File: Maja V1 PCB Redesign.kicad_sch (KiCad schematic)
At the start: 0 parts

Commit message: Add component
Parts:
- added F?: Polyfuse_Small, symbol Device:Polyfuse_Small
- added J1: TYPE-C-31-M-12, Keyboard Component:HRO_TYPE-C-31-M-12, symbol TYPE-C-31-M-12:TYPE-C-31-M-12
- added S?: SKQGAFE010, SW_SKQGAFE010, symbol SKQGAFE010:SKQGAFE010
- added U?: PRTR5V0U2X, symbol random-keyboard-parts:PRTR5V0U2X
- added Y?: Crystal_GND24_Small, symbol Device:Crystal_GND24_Small
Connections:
- new net: J1.S1 (SHIELD), J1.S2 (SHIELD), J1.S3 (SHIELD), J1.S4 (SHIELD)
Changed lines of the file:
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@@
-(kicad_sch (version 20210621) (generator eeschema)
+(kicad_sch (version 20211123) (generator eeschema)
   (paper "A4")
+  (symbol (lib_id "TYPE-C-31-M-12:TYPE-C-31-M-12") (at 63.5 78.74 0) (unit 1)
+    (in_bom yes) (on_board yes) (fields_autoplaced)
+    (property "Reference" "J1" (id 0) (at 63.5 60.96 0))
+    (property "Value" "TYPE-C-31-M-12" (id 1) (at 63.5 63.5 0))
+    (property "Footprint" "Keyboard Component:HRO_TYPE-C-31-M-12" (id 2) (at 90.17 50.8 0)
+      (effects (font (size 1.27 1.27)) (justify left bottom) hide)
+    )
+    (property "Datasheet" "" (id 3) (at 63.5 78.74 0)
+      (effects (font (size 1.27 1.27)) (justify left bottom) hide)
+    )
+    (property "MAXIMUM_PACKAGE_HEIGHT" "3.31mm" (id 4) (at 95.25 55.88 0)
+      (effects (font (size 1.27 1.27)) (justify left bottom) hide)
+    )
+    (property "MANUFACTURER" "HRO Electronics" (id 5) (at 93.98 57.15 0)
+      (effects (font (size 1.27 1.27)) (justify left bottom) hide)
+    )
+    (property "PARTREV" "A" (id 6) (at 63.5 78.74 0)
+      (effects (font (size 1.27 1.27)) (justify left bottom) hide)
+    )
+    (property "STANDARD" "Manufacturer Recommendations" (id 7) (at 91.44 53.34 0)
+      (effects (font (size 1.27 1.27)) (justify left bottom) hide)
+    )
+    (pin "A1B12")
+    (pin "A4B9")
+    (pin "A5")
+    (pin "A6")
+    (pin "A7")
+    (pin "A8")
+    (pin "B1A12")
+    (pin "B4A9")
+    (pin "B5")
+    (pin "B6")
+    (pin "B7")
+    (pin "B8")
+    (pin "S1")
+    (pin "S2")
+    (pin "S3")
+    (pin "S4")
+  )
+  (symbol (lib_id "Device:Polyfuse_Small") (at 113.03 58.42 0) (unit 1)
+    (in_bom yes) (on_board yes) (fields_autoplaced)
+    (property "Reference" "F?" (id 0) (at 115.57 57.1499 0)
+      (effects (font (size 1.27 1.27)) (justify left))
+    )
+    (property "Value" "Polyfuse_Small" (id 1) (at 115.57 59.6899 0)
+      (effects (font (size 1.27 1.27)) (justify left))
+    )
+    (property "Footprint" "" (id 2) (at 114.3 63.5 0)
+      (effects (font (size 1.27 1.27)) (justify left) hide)
+    )
+    (property "Datasheet" "~" (id 3) (at 113.03 58.42 0)
+      (effects (font (size 1.27 1.27)) hide)
+    )
+    (pin "1")
+    (pin "2")
+  )
+  (symbol (lib_id "SKQGAFE010:SKQGAFE010") (at 127 76.2 0) (unit 1)
+    (in_bom yes) (on_board yes) (fields_autoplaced)
+    (property "Reference" "S?" (id 0) (at 127 66.04 0))
+    (property "Value" "SKQGAFE010" (id 1) (at 127 68.58 0))
+    (property "Footprint" "SW_SKQGAFE010" (id 2) (at 127 76.2 0)
+      (effects (font (size 1.27 1.27)) (justify left bottom) hide)
+    )
+    (property "Datasheet" "" (id 3) (at 127 76.2 0)
+      (effects (font (size 1.27 1.27)) (justify left bottom) hide)
+    )
+    (property "PART_REV" "B1" (id 4) (at 127 76.2 0)
+      (effects (font (size 1.27 1.27)) (justify left bottom) hide)
+    )
+    (property "STANDARD" "MANUFACTURER RECOMMENDATIONS" (id 5) (at 127 76.2 0)
+      (effects (font (size 1.27 1.27)) (justify left bottom) hide)
+    )
+    (property "MANUFACTURER" "ALPS" (id 6) (at 127 76.2 0)
+      (effects (font (size 1.27 1.27)) (justify left bottom) hide)
+    )
+    (pin "1")
+    (pin "2")
+    (pin "3")
+    (pin "4")
+  )
+  (symbol (lib_id "random-keyboard-parts:PRTR5V0U2X") (at 162.56 77.47 0) (unit 1)
+    (in_bom yes) (on_board yes) (fields_autoplaced)
+    (property "Reference" "U?" (id 0) (at 162.56 69.85 0)
+      (effects (font (size 1.524 1.524)))
+    )
+    (property "Value" "PRTR5V0U2X" (id 1) (at 162.56 73.66 0)
+      (effects (font (size 1.524 1.524)))
+    )
+    (property "Footprint" "" (id 2) (at 162.56 77.47 0)
+      (effects (font (size 1.524 1.524)) hide)
+    )
+    (property "Datasheet" "" (id 3) (at 162.56 77.47 0)
+      (effects (font (size 1.524 1.524)) hide)
+    )
+    (pin "1")
+    (pin "2")
+    (pin "3")
+    (pin "4")
+  )
+  (symbol (lib_id "Device:Crystal_GND24_Small") (at 140.97 45.72 0) (unit 1)
+    (in_bom yes) (on_board yes) (fields_autoplaced)
+    (property "Reference" "Y?" (id 0) (at 153.67 41.5798 0))
+    (property "Value" "Crystal_GND24_Small" (id 1) (at 153.67 44.1198 0))
+    (property "Footprint" "" (id 2) (at 140.97 45.72 0)
+      (effects (font (size 1.27 1.27)) hide)
+    )
+    (property "Datasheet" "~" (id 3) (at 140.97 45.72 0)
+      (effects (font (size 1.27 1.27)) hide)
+    )
+    (pin "1")
+    (pin "2")
+    (pin "3")
+    (pin "4")
+  )
   (sheet_instances
     (path "/" (page "1"))
   )
+  (symbol_instances
+    (path "/6babdcfa-df8d-4f52-842d-5f83ac30f7ac"
+      (reference "F?") (unit 1) (value "Polyfuse_Small") (footprint "")
+    )
+    (path "/31ab6056-77a7-4722-90c3-619f8073b0cc"
+      (reference "J1") (unit 1) (value "TYPE-C-31-M-12") (footprint "Keyboard Component:HRO_TYPE-C-31-M-12")
+    )
+    (path "/9951f9e8-2210-4dce-85a6-75dc798cb094"
+      (reference "S?") (unit 1) (value "SKQGAFE010") (footprint "SW_SKQGAFE010")
+    )
+    (path "/a052622e-11d7-4538-81c6-88b46570ea55"
+      (reference "U?") (unit 1) (value "PRTR5V0U2X") (footprint "")
+    )
+    (path "/ad1125ce-e48c-4b3a-afc6-cc3f494ae7c7"
+      (reference "Y?") (unit 1) (value "Crystal_GND24_Small") (footprint "")
+    )
+  )
 )

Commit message: Atmega Schematic
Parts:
- added C? (x2): 22p, symbol Device:C_Small
- added C? (x5): 0.1u, symbol Device:C_Small
- added C?: 1u, symbol Device:C_Small
- added J?: AVR-ISP-6, symbol Connector:AVR-ISP-6
- added R? (x2): 5.1k, symbol Device:R_Small
- added R? (x2): 10k, symbol Device:R_Small
- added R? (x2): 22, symbol Device:R_Small
- added U1: ATmega32U4-M, Package_DFN_QFN:QFN-44-1EP_7x7mm_P0.5mm_EP5.2x5.2mm, symbol MCU_Microchip_ATmega:ATmega32U4-M
- F?: value Polyfuse_Small -> 500m
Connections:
- net GND: now reaches J1.A1B12 (GND)
- net GND: now also J1.B1A12 (GND), J1.S1 (SHIELD), J1.S2 (SHIELD), J1.S3 (SHIELD), J1.S4 (SHIELD), S?.3, U?.1 (GND), Y?.2, Y?.4, C?.2, C?.2, C?.2, C?.2, C?.2, C?.2, C?.2, C?.2, J?.6 (GND), R?.2, R?.2, R?.2, U1.15 (GND), U1.23 (GND), U1.35 (GND), U1.43 (GND), U1.45 (GND), U1.5 (UGND)
- net VCC: now reaches J1.A4B9 (VBUS)
- net VCC: now also F?.2, J1.B4A9 (VBUS), U?.4 (VCC)
- net at J1.A5 (CC1): now also R?.1
- net at J1.A6 (DP1): now also J1.B6 (DP2), U?.2 (IO1), R?.1
- net at J1.A7 (DN1): now also J1.B7 (DN2), U?.3 (IO2), R?.1
- net at J1.B5 (CC2): now also R?.1
- net +5V: now reaches F?.1
- net +5V: now also C?.1, C?.1, C?.1, C?.1, C?.1, J?.2 (VCC), R?.1, U1.14 (VCC), U1.2 (UVCC), U1.24 (AVCC), U1.34 (VCC), U1.44 (AVCC)
- net RESET: now reaches S?.2
- net RESET: now also J?.5 (~{RST}), R?.2, U1.13 (~{RESET})
- net XTAL1: now reaches Y?.1
- net XTAL1: now also C?.1, U1.17 (XTAL1)
- net XTAL2: now reaches Y?.3
- net XTAL2: now also C?.1, U1.16 (XTAL2)
- new net: R?.1, U1.33 (~{HWB}/PE2)
- new net: C?.1, U1.6 (UCAP)
- new net D+: R?.2, U1.4 (D+)
- new net D-: R?.2, U1.3 (D-)
- new net MISO: J?.1 (MISO), U1.11 (PB3)
- new net MOSI: J?.4 (MOSI), U1.10 (PB2)
- new net SCK: J?.3 (SCK), U1.9 (PB1)
- no-connect marks 0 -> 5
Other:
- moved on the sheet: F?, J1, S?, U?, Y?

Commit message: Finish Wiring
Schematic wiring
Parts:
- gave numbers to parts that had none: 19
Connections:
- net +5V: now also U1.7 (VBUS)
- net ROW0: now reaches U1.1 (PE6)
- net ROW 2: now reaches U1.12 (PB7)
- net COL0: now reaches U1.18 (PD0)
- net COL1: now reaches U1.19 (PD1)
- net COL2: now reaches U1.20 (PD2)
- net COL3: now reaches U1.21 (PD3)
- net COL5: now reaches U1.22 (PD5)
- net COL4: now reaches U1.25 (PD4)
- net COL6: now reaches U1.26 (PD6)
- net ROW4: now reaches U1.28 (PB4)
- net ROW3: now reaches U1.29 (PB5)
- net COL13: now reaches U1.30 (PB6)
- net COL15: now reaches U1.31 (PC6)
- net COL14: now reaches U1.32 (PC7)
- net COL12: now reaches U1.36 (PF7)
- net COL11: now reaches U1.37 (PF6)
- net COL10: now reaches U1.38 (PF5)
- net COL9: now reaches U1.39 (PF4)
- net COL8: now reaches U1.40 (PF1)
- net COL7: now reaches U1.41 (PF0)
- net ROW1: now reaches U1.8 (PB0)
- no-connect marks 5 -> 6
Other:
- added sheet Matrix (Matrix.kicad_sch)

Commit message: fixed footprint & Symbol
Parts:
- C1, C2, C3, C4, C5, C6, C7, C8: footprint (none) -> Capacitor_SMD:C_0805_2012Metric_Pad1.18x1.45mm_HandSolder
- F1: footprint (none) -> Fuse:Fuse_1206_3216Metric_Pad1.42x1.75mm_HandSolder
- J2: footprint (none) -> random-keyboard-parts:Reset_Pretty
- R1, R2, R3, R4, R5, R6: footprint (none) -> Resistor_SMD:R_0805_2012Metric_Pad1.20x1.40mm_HandSolder
- U2: footprint (none) -> random-keyboard-parts:SOT143B
- Y1: footprint (none) -> Crystal:Crystal_SMD_3225-4Pin_3.2x2.5mm

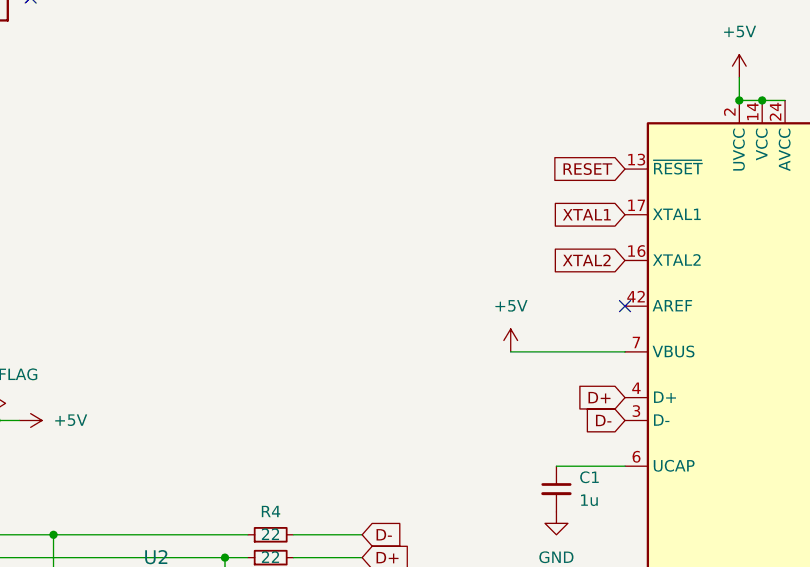
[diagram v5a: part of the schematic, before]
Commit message: add JST
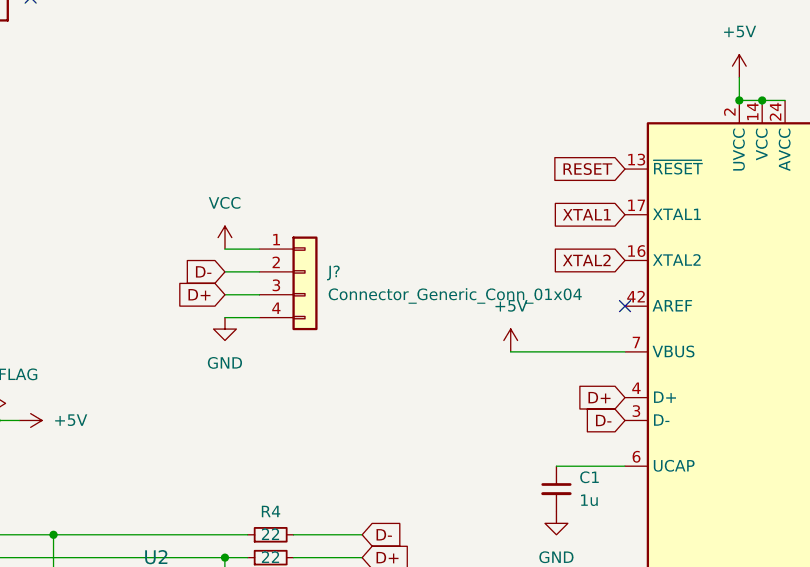
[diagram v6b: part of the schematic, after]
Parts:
- added J?: Connector_Generic_Conn_01x04, symbol Unified-Daughterboard-cache:Connector_Generic_Conn_01x04
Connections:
- net D+: now also J?.3 (Pin_3)
- net D-: now also J?.2 (Pin_2)
- net GND: now also J?.4 (Pin_4)
- net VCC: now also J?.1 (Pin_1)
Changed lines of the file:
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@@
+    (stroke (width 0) (type default) (color 0 0 0 0))
+  )
+  (wire (pts (xy 100.33 69.85) (xy 104.14 69.85))
     (stroke (width 0) (type default) (color 0 0 0 0))
   )
@@
     (stroke (width 0) (type default) (color 0 0 0 0))
   )
+  (wire (pts (xy 100.33 72.39) (xy 104.14 72.39))
+    (stroke (width 0) (type default) (color 0 0 0 0))
+  )
   (wire (pts (xy 63.5 93.98) (xy 63.5 99.06))
     (stroke (width 0) (type default) (color 0 0 0 0))
@@
     (stroke (width 0) (type default) (color 0 0 0 0))
   )
+  (wire (pts (xy 100.33 74.93) (xy 104.14 74.93))
+    (stroke (width 0) (type default) (color 0 0 0 0))
+  )
   (wire (pts (xy 160.02 50.8) (xy 162.56 50.8))
     (stroke (width 0) (type default) (color 0 0 0 0))
@@
   )
   (wire (pts (xy 175.26 96.52) (xy 177.8 96.52))
+    (stroke (width 0) (type default) (color 0 0 0 0))
+  )
+  (wire (pts (xy 100.33 67.31) (xy 104.14 67.31))
     (stroke (width 0) (type default) (color 0 0 0 0))
   )
@@
     )
   )
+  (global_label "D-" (shape input) (at 100.33 69.85 180) (fields_autoplaced)
+    (effects (font (size 1.27 1.27)) (justify right))
+    (property "Intersheet References" "${INTERSHEET_REFS}" (id 0) (at 95.0745 69.7706 0)
+      (effects (font (size 1.27 1.27)) (justify right) hide)
+    )
+  )
   (global_label "SCK" (shape input) (at 219.71 30.48 0) (fields_autoplaced)
     (effects (font (size 1.27 1.27)) (justify left))
@@
     (property "Intersheet References" "${INTERSHEET_REFS}" (id 0) (at 183.9626 60.8806 0)
       (effects (font (size 1.27 1.27)) (justify left) hide)
+    )
+  )
+  (global_label "D+" (shape input) (at 100.33 72.39 180) (fields_autoplaced)
+    (effects (font (size 1.27 1.27)) (justify right))
+    (property "Intersheet References" "${INTERSHEET_REFS}" (id 0) (at 95.0745 72.3106 0)
+      (effects (font (size 1.27 1.27)) (justify right) hide)
     )
   )
@@
     (pin "S4")
   )
+  (symbol (lib_id "Unified-Daughterboard-cache:Connector_Generic_Conn_01x04") (at 109.22 69.85 0) (unit 1)
+    (in_bom yes) (on_board yes) (fields_autoplaced)
+    (property "Reference" "J?" (id 0) (at 111.76 69.8499 0)
+      (effects (font (size 1.27 1.27)) (justify left))
+    )
+    (property "Value" "Connector_Generic_Conn_01x04" (id 1) (at 111.76 72.3899 0)
+      (effects (font (size 1.27 1.27)) (justify left))
+    )
+    (property "Footprint" "" (id 2) (at 109.22 69.85 0)
+      (effects (font (size 1.27 1.27)) hide)
+    )
+    (property "Datasheet" "" (id 3) (at 109.22 69.85 0)
+      (effects (font (size 1.27 1.27)) hide)
+    )
+    (pin "1")
+    (pin "2")
+    (pin "3")
+    (pin "4")
+  )
   (symbol (lib_id "power:GND") (at 190.5 111.76 0) (unit 1)
     (in_bom yes) (on_board yes) (fields_autoplaced)
@@
     (pin "1")
     (pin "2")
+  )
+  (symbol (lib_id "power:VCC") (at 100.33 67.31 0) (unit 1)
+    (in_bom yes) (on_board yes) (fields_autoplaced)
+    (property "Reference" "#PWR?" (id 0) (at 100.33 71.12 0)
+      (effects (font (size 1.27 1.27)) hide)
+    )
+    (property "Value" "VCC" (id 1) (at 100.33 62.23 0))
+    (property "Footprint" "" (id 2) (at 100.33 67.31 0)
+      (effects (font (size 1.27 1.27)) hide)
+    )
+    (property "Datasheet" "" (id 3) (at 100.33 67.31 0)
+      (effects (font (size 1.27 1.27)) hide)
+    )
+    (pin "1")
+  )
+  (symbol (lib_id "power:GND") (at 100.33 74.93 0) (unit 1)
+    (in_bom yes) (on_board yes) (fields_autoplaced)
+    (property "Reference" "#PWR?" (id 0) (at 100.33 81.28 0)
+      (effects (font (size 1.27 1.27)) hide)
+    )
+    (property "Value" "GND" (id 1) (at 100.33 80.01 0))
+    (property "Footprint" "" (id 2) (at 100.33 74.93 0)
+      (effects (font (size 1.27 1.27)) hide)
+    )
+    (property "Datasheet" "" (id 3) (at 100.33 74.93 0)
+      (effects (font (size 1.27 1.27)) hide)
+    )
+    (pin "1")
   )
   (symbol (lib_id "power:+5V") (at 132.08 78.74 0) (unit 1)
@@
       (reference "#PWR0116") (unit 1) (value "+5V") (footprint "")
     )
+    (path "/468ba756-b608-4ef3-b75b-cee3864ffcfd"
+      (reference "#PWR?") (unit 1) (value "VCC") (footprint "")
+    )
+    (path "/47139887-f780-4c14-afae-8d820d1e0de6"
+      (reference "#PWR?") (unit 1) (value "GND") (footprint "")
+    )
     (path "/43d87709-5a30-4180-96d5-6f8b8ffdfd1d"
       (reference "C1") (unit 1) (value "1u") (footprint "Capacitor_SMD:C_0805_2012Metric_Pad1.18x1.45mm_HandSolder")
@@
       (reference "J2") (unit 1) (value "AVR-ISP-6") (footprint "random-keyboard-parts:Reset_Pretty")
     )
+    (path "/361725fc-4f2d-472a-8075-f63ed1495c22"
+      (reference "J?") (unit 1) (value "Connector_Generic_Conn_01x04") (footprint "")
+    )
     (path "/4526e43e-053f-4520-ab68-78d672909c1b/574f6d28-bfb7-4f6c-b7f3-59d6bbd5a2c5"

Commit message: MCU
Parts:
- J3: renamed from J?; footprint (none) -> Connector_JST:JST_SH_SM04B-SRSS-TB_1x04-1MP_P1.00mm_Horizontal
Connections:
- net COL0: now also U1.41 (PF0); no longer U1.18 (PD0)
- net COL1: now also U1.40 (PF1); no longer U1.19 (PD1)
- net COL10: now also U1.21 (PD3); no longer U1.38 (PF5)
- net COL11: now also U1.22 (PD5); no longer U1.37 (PF6)
- net COL12: now also U1.25 (PD4); no longer U1.36 (PF7)
- net COL13: now also U1.26 (PD6); no longer U1.30 (PB6)
- net COL14: now also U1.27 (PD7); no longer U1.32 (PC7)
- net COL15: now also U1.28 (PB4); no longer U1.31 (PC6)
- net COL2: now also U1.39 (PF4); no longer U1.20 (PD2)
- net COL3: now also U1.38 (PF5); no longer U1.21 (PD3)
- net COL4: now also U1.37 (PF6); no longer U1.25 (PD4)
- net COL5: now also U1.36 (PF7); no longer U1.22 (PD5)
- net COL6: now also U1.32 (PC7); no longer U1.26 (PD6)
- net COL7: now also U1.18 (PD0); no longer U1.41 (PF0)
- net COL8: now also U1.19 (PD1); no longer U1.40 (PF1)
- net COL9: now also U1.20 (PD2); no longer U1.39 (PF4)
- net ROW4: now also U1.30 (PB6); no longer U1.28 (PB4)

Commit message: tracing 1
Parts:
- C3, C4, C6, C7: value 0.1u -> 100nF
- C8: value 0.1u -> 10uF
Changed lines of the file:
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@@
       (effects (font (size 1.27 1.27)) (justify left))
     )
-    (property "Value" "0.1u" (id 1) (at 260.35 140.9762 0)
+    (property "Value" "100nF" (id 1) (at 260.35 140.9762 0)
       (effects (font (size 1.27 1.27)) (justify left))
     )
@@
       (effects (font (size 1.27 1.27)) (justify left))
     )
-    (property "Value" "0.1u" (id 1) (at 266.7 140.9762 0)
+    (property "Value" "10uF" (id 1) (at 266.7 140.9762 0)
       (effects (font (size 1.27 1.27)) (justify left))
     )
@@
       (effects (font (size 1.27 1.27)) (justify left))
     )
-    (property "Value" "0.1u" (id 1) (at 245.11 140.9762 0)
+    (property "Value" "100nF" (id 1) (at 245.11 140.9762 0)
       (effects (font (size 1.27 1.27)) (justify left))
     )
@@
       (effects (font (size 1.27 1.27)) (justify left))
     )
-    (property "Value" "0.1u" (id 1) (at 237.49 140.9762 0)
+    (property "Value" "100nF" (id 1) (at 237.49 140.9762 0)
       (effects (font (size 1.27 1.27)) (justify left))
     )
@@
       (effects (font (size 1.27 1.27)) (justify left))
     )
-    (property "Value" "0.1u" (id 1) (at 252.73 140.9762 0)
+    (property "Value" "100nF" (id 1) (at 252.73 140.9762 0)
       (effects (font (size 1.27 1.27)) (justify left))
     )
@@
     )
     (path "/c21145b3-2ba8-4199-bd62-8a52576b0f76"
-      (reference "C3") (unit 1) (value "0.1u") (footprint "Capacitor_SMD:C_0805_2012Metric_Pad1.18x1.45mm_HandSolder")
+      (reference "C3") (unit 1) (value "100nF") (footprint "Capacitor_SMD:C_0805_2012Metric_Pad1.18x1.45mm_HandSolder")
     )
     (path "/9d000907-1470-4798-b9e7-26b248406d6f"
-      (reference "C4") (unit 1) (value "0.1u") (footprint "Capacitor_SMD:C_0805_2012Metric_Pad1.18x1.45mm_HandSolder")
+      (reference "C4") (unit 1) (value "100nF") (footprint "Capacitor_SMD:C_0805_2012Metric_Pad1.18x1.45mm_HandSolder")
     )
     (path "/1276ab35-37a9-4274-924a-3f362baae999"
@@
     )
     (path "/e770da12-986a-45ad-a103-4032138ba68c"
-      (reference "C6") (unit 1) (value "0.1u") (footprint "Capacitor_SMD:C_0805_2012Metric_Pad1.18x1.45mm_HandSolder")
+      (reference "C6") (unit 1) (value "100nF") (footprint "Capacitor_SMD:C_0805_2012Metric_Pad1.18x1.45mm_HandSolder")
     )
     (path "/3ac248b7-9e44-4505-a10b-038b9a847ccd"
-      (reference "C7") (unit 1) (value "0.1u") (footprint "Capacitor_SMD:C_0805_2012Metric_Pad1.18x1.45mm_HandSolder")
+      (reference "C7") (unit 1) (value "100nF") (footprint "Capacitor_SMD:C_0805_2012Metric_Pad1.18x1.45mm_HandSolder")
     )
     (path "/51a0a7d6-1fa8-4005-93e7-e1b2ea207058"
-      (reference "C8") (unit 1) (value "0.1u") (footprint "Capacitor_SMD:C_0805_2012Metric_Pad1.18x1.45mm_HandSolder")
+      (reference "C8") (unit 1) (value "10uF") (footprint "Capacitor_SMD:C_0805_2012Metric_Pad1.18x1.45mm_HandSolder")
     )
     (path "/4526e43e-053f-4520-ab68-78d672909c1b/f5efab71-2392-4dcb-bb10-ddbe2952ed8d"
